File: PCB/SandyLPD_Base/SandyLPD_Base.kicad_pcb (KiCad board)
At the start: 2 copper layers, 271.5 x 101 mm, 242 parts, among them J1 Conn_02x02_Odd_Even, J10 Conn_01x10_Pin, J11 Conn_01x03, J2 Conn_01x03, J4 Conn_01x10_Pin, J5 USB_C_Receptacle_USB2.0, J6 USB_C_Receptacle_USB2.0, J7 USB_C_Receptacle_USB2.0, J8 USB_C_Receptacle_USB2.0, J9 Conn_02x02_Odd_Even, SW1 BOOT_ALT, SW2 RESET_ALT, SW3 SW_DIP_x04, SW4 BOOT_ALT, SW5 RESET_ALT, SW6 SW_DIP_x04, U1 NCP1117-3.3_SOT223, U2 NCP1117-3.3_SOT223, U3 RP2040, U4 W25Q128JVPIQ, U5 RP2040, U6 W25Q128JVPIQ, Y1 12MHz, Y2 12MHz

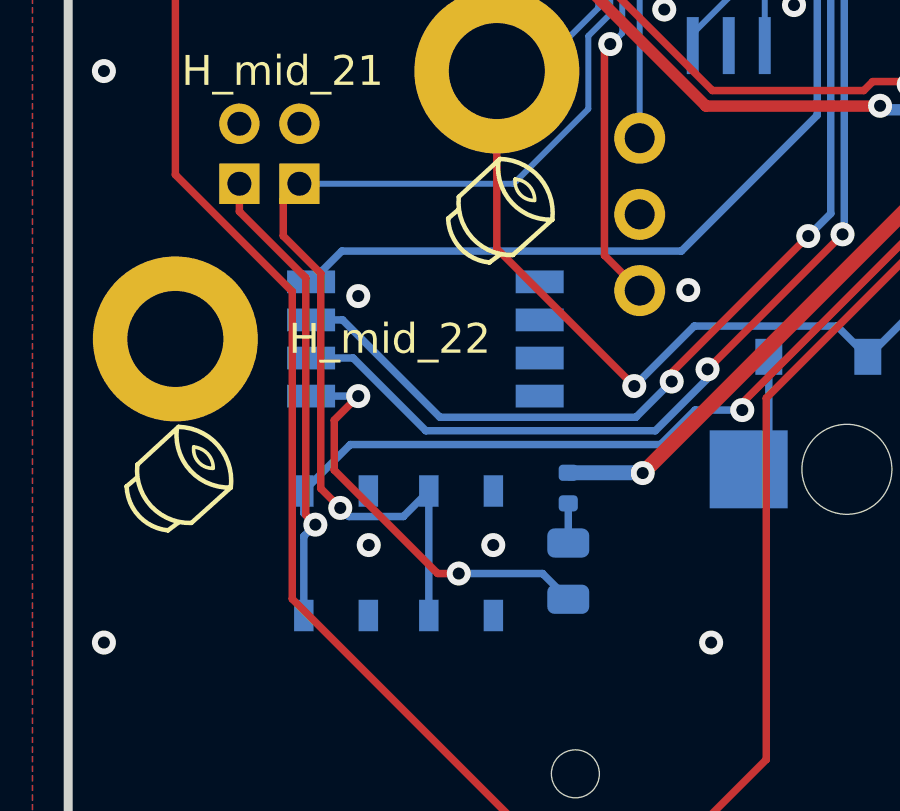
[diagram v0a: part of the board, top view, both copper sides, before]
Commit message: リセットスイッチ、電源LEDの位置を、左右で合わせてボトムBの切り欠きに収まるように調整。
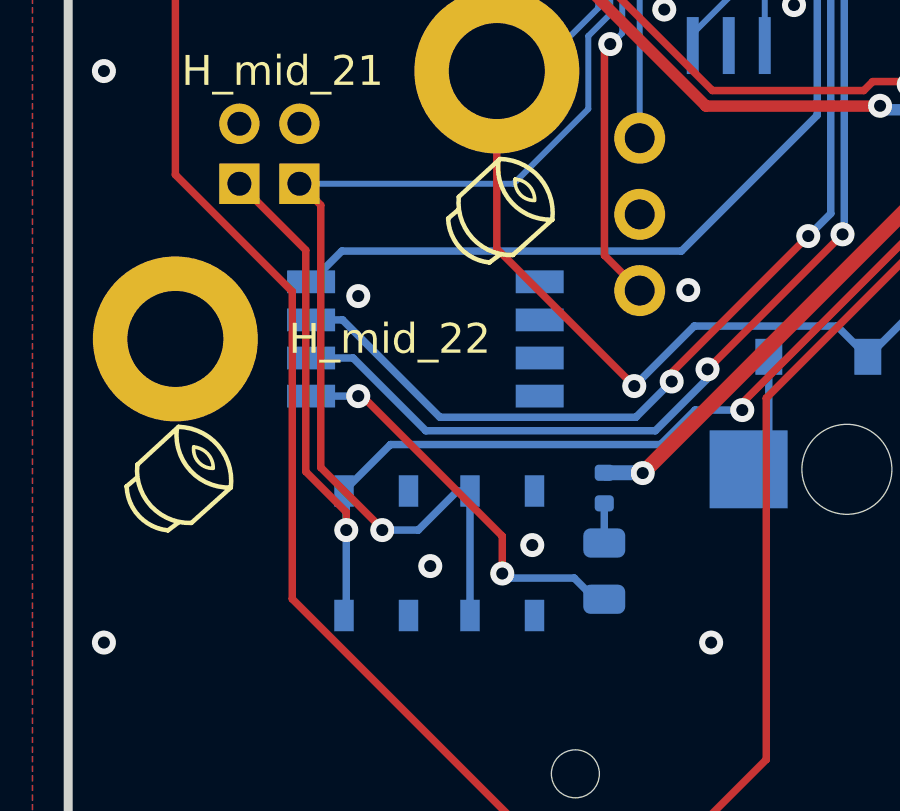
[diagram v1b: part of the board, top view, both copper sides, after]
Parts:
- moved SW5 1.37 mm to (178.4, 90.7)
- moved SW4 1.34 mm to (174.2, 90.7)
- moved R7 1.20 mm to (181.8, 88.5)
- moved STLED2 1.20 mm to (181.8, 91.3)
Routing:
- net +3V3_R: track 103.0 -> 101.8 mm
- net R_USB_BOOT: track 73.6 -> 72.6 mm
- net R_RESET: track 38.9 -> 39.8 mm
- net PowerLED_R: track 14.0 -> 13.3 mm

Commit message: シルク位置調整 #20
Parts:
- moved REF** 3.82 mm to (173.4, 38.5)
- moved REF** 3.77 mm to (147.3, 87.1)
- moved REF** 3.77 mm to (288.4, 56.2)
- moved REF** 3.04 mm to (147.9, 56.8)
- moved REF** 2.66 mm to (169.9, 87.1)
- moved REF** 2.66 mm to (169.9, 56.2)
- moved REF** 0.94 mm to (145.0, 38.5)
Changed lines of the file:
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@@
 		(tags "mounting hole 2.2mm m2")
 		(property "Reference" "H_mid_15"
-			(at 7.14376 0.000006 0)
+			(at 6.548447 -0.595307 0)
 			(layer "F.SilkS")
 			(effects
@@
 		(locked yes)
 		(layer "F.Cu")
-		(at 145.478846 37.719031)
+		(at 145.002185 38.528405)
 		(property "Reference" "REF**"
 			(at 0 -0.5 0)
@@
 		(fp_arc
 			(start 0.104982 -1.833316)
-			(mid 1.427206 -1.208666)
+			(mid 1.427205 -1.208666)
 			(end 1.847522 0.191975)
 			(stroke
@@
 		(fp_arc
 			(start 0.104982 -1.833316)
-			(mid 1.427206 -1.208666)
+			(mid 1.427205 -1.208666)
 			(end 1.847522 0.191975)
 			(stroke
@@
 		(fp_arc
 			(start 0.104982 -1.833316)
-			(mid 1.427206 -1.208666)
+			(mid 1.427205 -1.208666)
 			(end 1.847522 0.191975)
 			(stroke
@@
 		(tags "mounting hole 2.2mm m2")
 		(property "Reference" "H_mid_13"
-			(at 7.143752 -0.000006 0)
+			(at 6.548439 0.595307 0)
 			(layer "F.SilkS")
 			(effects
@@
 		(tags "mounting hole 2.2mm m2")
 		(property "Reference" "H_mid_16"
-			(at -7.14376 -0.000006 0)
+			(at -6.548447 0.595307 0)
 			(layer "F.SilkS")
 			(effects
@@
 		(fp_arc
 			(start 0.104982 -1.833316)
-			(mid 1.427206 -1.208666)
+			(mid 1.427205 -1.208666)
 			(end 1.847522 0.191975)
 			(stroke
@@
 		(locked yes)
 		(layer "F.Cu")
-		(at 150.836663 88.320636)
+		(at 147.264785 87.13001)
 		(property "Reference" "REF**"
 			(at 0 -0.5 0)
@@
 		(fp_arc
 			(start 0.104982 -1.833316)
-			(mid 1.427206 -1.208666)
+			(mid 1.427205 -1.208666)
 			(end 1.847522 0.191975)
 			(stroke
@@
 		(fp_arc
 			(start 0.104982 -1.833316)
-			(mid 1.427206 -1.208666)
+			(mid 1.427205 -1.208666)
 			(end 1.847522 0.191975)
 			(stroke
@@
 		(tags "mounting hole 2.2mm m2")
 		(property "Reference" "H_mid_1"
-			(at 6.548439 -0.000001 0)
+			(at 5.953126 1.785938 0)
 			(layer "F.SilkS")
 			(effects
@@
 		(fp_arc
 			(start 0.104982 -1.833316)
-			(mid 1.427206 -1.208666)
+			(mid 1.427205 -1.208666)
 			(end 1.847522 0.191975)
 			(stroke
@@
 		(tags "mounting hole 2.2mm m2")
 		(property "Reference" "H_mid_5"
-			(at -6.548447 -0.595319 0)
+			(at -6.039169 0.59062 0)
 			(layer "F.SilkS")
 			(effects
@@
 		(locked yes)
 		(layer "F.Cu")
-		(at 172.863244 34.742466)
+		(at 173.402185 38.528405)
 		(property "Reference" "REF**"
 			(at 0 -0.5 0)
@@
 		(fp_arc
 			(start 0.104982 -1.833316)
-			(mid 1.427206 -1.208666)
+			(mid 1.427205 -1.208666)
 			(end 1.847522 0.191975)
 			(stroke
@@
 		(tags "mounting hole 2.2mm m2")
 		(property "Reference" "H_mid_12"
-			(at -5.950341 -2.381246 0)
+			(at -6.548439 -0.595307 0)
 			(layer "F.SilkS")
 			(effects
@@
 		(locked yes)
 		(layer "F.Cu")
-		(at 167.505427 57.36436)
+		(at 169.886679 56.173734)
 		(property "Reference" "REF**"
 			(at 0 -0.5 0)
@@
 		(fp_arc
 			(start 0.104982 -1.833316)
-			(mid 1.427206 -1.208666)
+			(mid 1.427205 -1.208666)
 			(end 1.847522 0.191975)
 			(stroke
@@
 		(fp_arc
 			(start 0.104982 -1.833316)
-			(mid 1.427206 -1.208666)
+			(mid 1.427205 -1.208666)
 			(end 1.847522 0.191975)
 			(stroke
@@
 		(tags "mounting hole 2.2mm m2")
 		(property "Reference" "H_mid_21"
-			(at 7.14376 0.000006 0)
+			(at 6.548447 0.000006 0)
 			(layer "F.SilkS")
 			(effects
@@
 		(fp_arc
 			(start 9.525004 30.885971)
-			(mid 6.157414 29.491062)
+			(mid 6.157411 29.491063)
 			(end 4.762504 26.123471)
 			(stroke
@@
 		(locked yes)
 		(layer "F.Cu")
-		(at 167.505427 88.320636)
+		(at 169.886679 87.13001)
 		(property "Reference" "REF**"
 			(at 0 -0.5 0)
@@
 		(fp_arc
 			(start 0.104982 -1.833316)
-			(mid 1.427206 -1.208666)
+			(mid 1.427205 -1.208666)
 			(end 1.847522 0.191975)
 			(stroke
@@
 		(fp_arc
 			(start 0.104982 -1.833316)
-			(mid 1.427206 -1.208666)
+			(mid 1.427205 -1.208666)
 			(end 1.847522 0.191975)
 			(stroke
@@
 		(tags "mounting hole 2.2mm m2")
 		(property "Reference" "H_mid_14"
-			(at 7.143752 -0.000006 0)
+			(at 6.548439 0.595307 0)
 			(layer "F.SilkS")
 			(effects
@@
 		(fp_arc
 			(start 0.104982 -1.833316)
-			(mid 1.427206 -1.208666)
+			(mid 1.427205 -1.208666)
 			(end 1.847522 0.191975)
 			(stroke
@@
 		(locked yes)
 		(layer "F.Cu")
-		(at 291.925844 57.36436)
+		(at 288.353966 56.173734)
 		(property "Reference" "REF**"
 			(at 0 -0.5 0)
@@
 		(fp_arc
 			(start 0.104982 -1.833316)
-			(mid 1.427206 -1.208666)
+			(mid 1.427205 -1.208666)
 			(end 1.847522 0.191975)
 			(stroke
@@
 		(fp_arc
 			(start 0.104982 -1.833316)
-			(mid 1.427206 -1.208666)
+			(mid 1.427205 -1.208666)
 			(end 1.847522 0.191975)
 			(stroke
@@
 		(fp_arc
 			(start 0.104982 -1.833316)
-			(mid 1.427206 -1.208666)
+			(mid 1.427205 -1.208666)
 			(end 1.847522 0.191975)
 			(stroke
@@
 		(tags "mounting hole 2.2mm m2")
 		(property "Reference" "H_mid_3"
-			(at -6.548447 -0.000006 0)
+			(at -5.953134 1.785933 0)
 			(layer "F.SilkS")
 			(effects
@@
 		(fp_arc
 			(start 0.104982 -1.833316)
-			(mid 1.427206 -1.208666)
+			(mid 1.427205 -1.208666)
 			(end 1.847522 0.191975)
 			(stroke
@@
 		(locked yes)
 		(layer "F.Cu")
-		(at 150.836663 57.36436)
+		(at 147.860098 56.769047)
 		(property "Reference" "REF**"
 			(at 0 -0.5 0)
@@
 		(fp_arc
 			(start 0.104982 -1.833316)
-			(mid 1.427206 -1.208666)
+			(mid 1.427205 -1.208666)
 			(end 1.847522 0.191975)
 			(stroke
@@
 		(fp_arc
 			(start 0.104982 -1.833316)
-			(mid 1.427206 -1.208666)
+			(mid 1.427205 -1.208666)
 			(end 1.847522 0.191975)
 			(stroke
@@
 		(tags "mounting hole 2.2mm m2")
 		(property "Reference" "H_mid_4"
-			(at -6.548447 -0.000006 0)
+			(at -5.953134 1.785933 0)
 			(layer "F.SilkS")
 			(effects
@@
 		(fp_arc
 			(start 0.104982 -1.833316)
-			(mid 1.427206 -1.208666)
+			(mid 1.427205 -1.208666)
 			(end 1.847522 0.191975)
 			(stroke
@@
 		(tags "mounting hole 2.2mm m2")
 		(property "Reference" "H_mid_2"
-			(at -6.548447 -0.000006 0)
+			(at -5.953134 1.785933 0)
 			(layer "F.SilkS")
 			(effects
@@
 		(fp_arc
 			(start 0.104982 -1.833316)
-			(mid 1.427206 -1.208666)
+			(mid 1.427205 -1.208666)
 			(end 1.847522 0.191975)
 			(stroke
@@
 		(fp_arc
 			(start 0.104982 -1.833316)
-			(mid 1.427206 -1.208666)
+			(mid 1.427205 -1.208666)
 			(end 1.847522 0.191975)
 			(stroke
@@
 	)
 	(gr_text "Computer"
-		(at 135.358435 42.48153 0)
+		(at 135.358525 41.328405 180)
 		(layer "F.SilkS" knockout)
 		(effects
@@
 	)
 	(gr_text "Device"
-		(at 143.69281 43.672155 -90)
-		(layer "F.SilkS" knockout)
+		(at 151.002185 43.728405 90)
+		(layer "F.SilkS")
 		(effects
 			(font
@@
 	)
 	(gr_text "Computer"
-		(at 182.983435 42.48153 0)
+		(at 183.202185 41.328405 180)
 		(layer "F.SilkS" knockout)
 		(effects
@@
 	)
 	(gr_text "Device"
-		(at 174.64906 43.672155 90)
-		(layer "F.SilkS" knockout)
+		(at 167.302185 43.672155 270)
+		(layer "F.SilkS")
 		(effects
 			(font

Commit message: シルク位置調整 #20
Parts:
- moved REF** 6.33 mm to (42.5, 46.1)
- moved REF** 6.33 mm to (275.9, 46.1)
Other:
- board text added: "L Back"
- board text added: "R Back"
- board text removed: "Left 左 Back Side"
- board text removed: "Right 右 Back Side"
